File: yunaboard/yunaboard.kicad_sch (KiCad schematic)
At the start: 49 parts, among them J1 USB-C Receptacle USB 2.0, J2 JTAG/SWD Tag Connect, J3 PCB ANT, J4 GPIO Header 1, J5 GPIO Header 2, U1 ESP32-S3, U2 CP2102N-Axx-xQFN28, U3 USBLC6-2SC6, U4 MIC5365-3.3YD5, Y1 40 MHz (±10ppm)

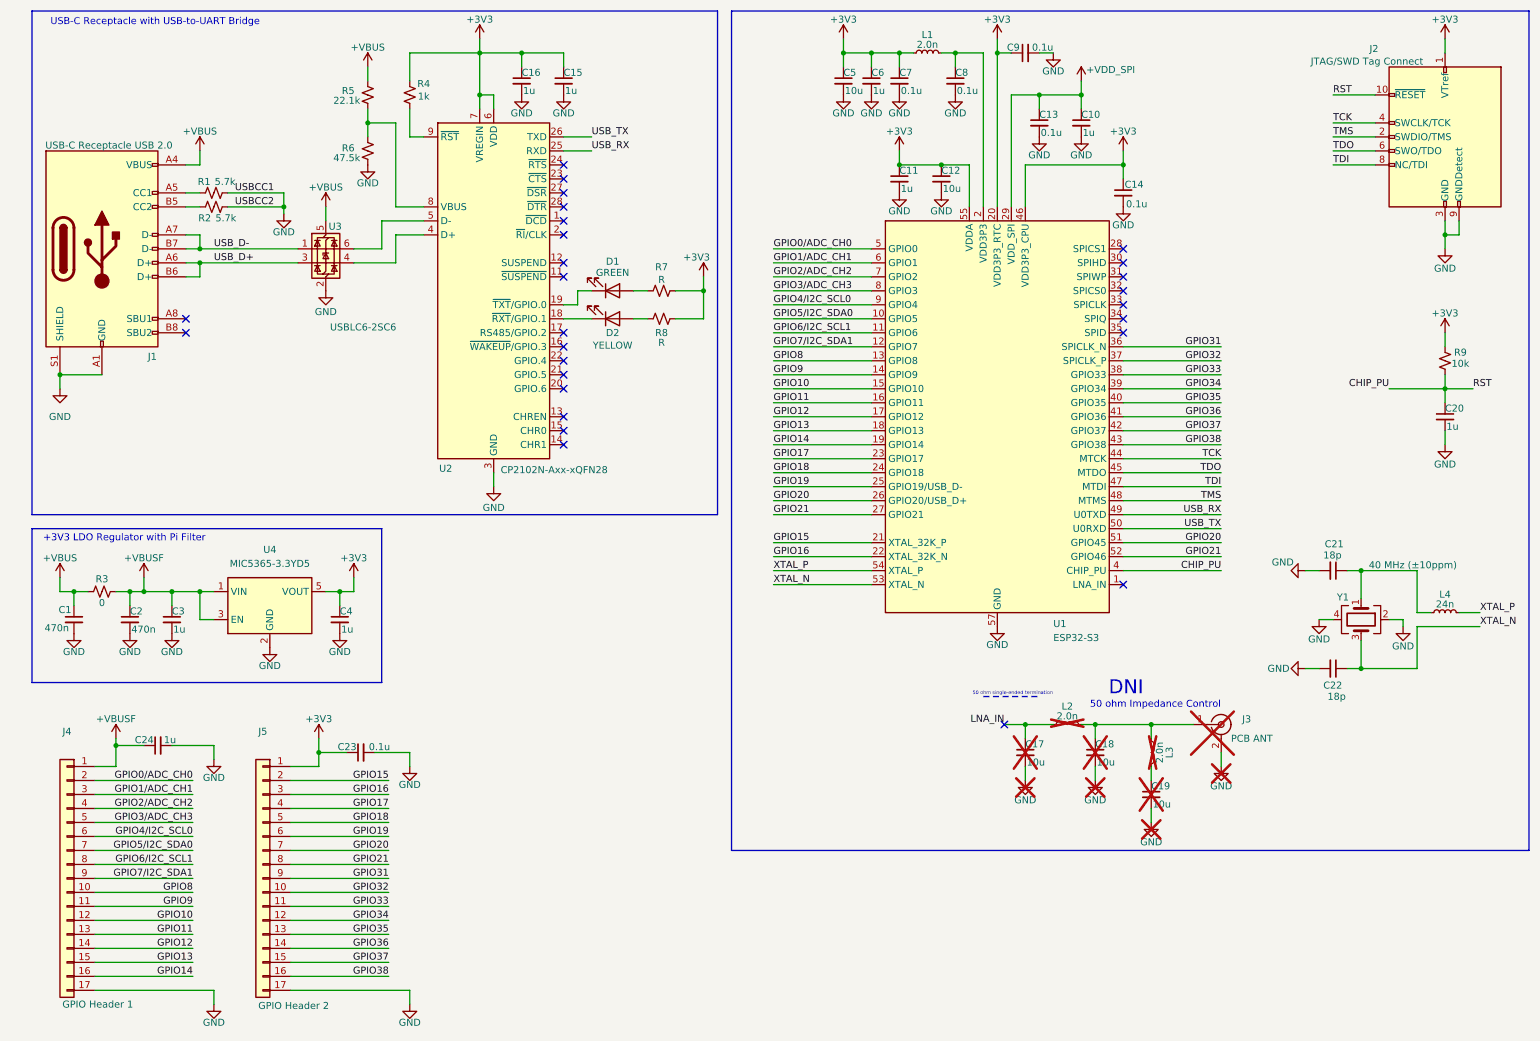
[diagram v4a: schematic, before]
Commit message: Update
- Changed JTAG connector to pin header for SWD
- Changed GPIO pin headers from 1mm length to 2mm length
- Adjusted the layout of the PCB from the initial design
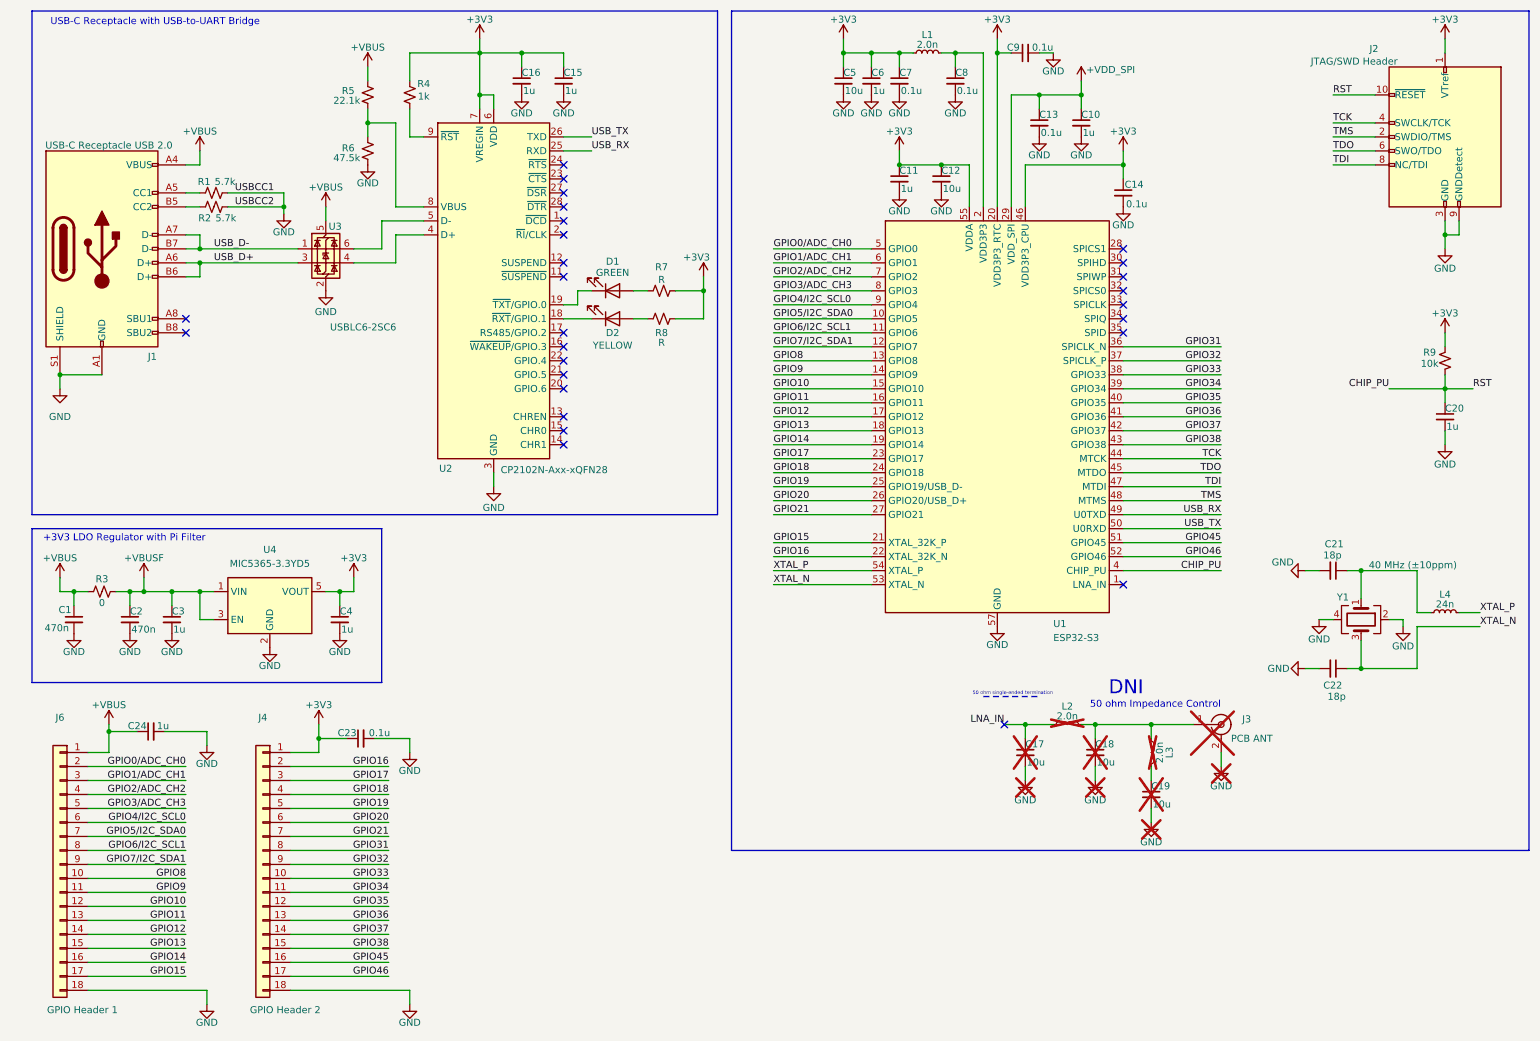
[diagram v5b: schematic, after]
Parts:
- removed J4: GPIO Header 1, Connector_PinHeader_1.00mm:PinHeader_1x17_P1.00mm_Vertical, symbol Connector_Generic:Conn_01x17
- removed J5: GPIO Header 2, Connector_PinHeader_1.00mm:PinHeader_1x17_P1.00mm_Vertical, symbol Connector_Generic:Conn_01x17
- added J4: GPIO Header 2, Connector_PinHeader_2.00mm:PinHeader_1x18_P2.00mm_Vertical, symbol Connector_Generic:Conn_01x18
- added J6: GPIO Header 1, Connector_PinHeader_2.00mm:PinHeader_1x18_P2.00mm_Vertical, symbol Connector_Generic:Conn_01x18
- J2: value JTAG/SWD Tag Connect -> JTAG/SWD Header; footprint Connector:Tag-Connect_TC2070-IDC-FP_2x07_P1.27mm_Vertical -> Connector_PinHeader_1.27mm:PinHeader_2x06_P1.27mm_Vertical
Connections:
- net +3V3: now also J4.1 (Pin_1)
- net +VBUS: now also C24.1, J6.1 (Pin_1)
- net +VBUSF: no longer C24.1
- net GND: now also J4.18 (Pin_18), J6.18 (Pin_18)
- net GPIO0/ADC_CH0: now also J6.2 (Pin_2)
- net GPIO10: now also J6.12 (Pin_12)
- net GPIO11: now also J6.13 (Pin_13)
- net GPIO12: now also J6.14 (Pin_14)
- net GPIO13: now also J6.15 (Pin_15)
- net GPIO14: now also J6.16 (Pin_16)
- net GPIO15: now also J6.17 (Pin_17)
- net GPIO16: now also J4.2 (Pin_2)
- net GPIO17: now also J4.3 (Pin_3)
- net GPIO18: now also J4.4 (Pin_4)
- net GPIO19: now also J4.5 (Pin_5)
- net GPIO1/ADC_CH1: now also J6.3 (Pin_3)
- net GPIO20: now also J4.6 (Pin_6); no longer U1.51 (GPIO45)
- net GPIO21: now also J4.7 (Pin_7); no longer U1.52 (GPIO46)
- net GPIO2/ADC_CH2: now also J6.4 (Pin_4)
- net GPIO31: now also J4.8 (Pin_8)
- net GPIO32: now also J4.9 (Pin_9)
- net GPIO33: now also J4.10 (Pin_10)
- net GPIO34: now also J4.11 (Pin_11)
- net GPIO35: now also J4.12 (Pin_12)
- net GPIO36: now also J4.13 (Pin_13)
- net GPIO37: now also J4.14 (Pin_14)
- net GPIO38: now also J4.15 (Pin_15)
- net GPIO3/ADC_CH3: now also J6.5 (Pin_5)
- net GPIO4/I2C_SCL0: now also J6.6 (Pin_6)
- net GPIO5/I2C_SDA0: now also J6.7 (Pin_7)
- net GPIO6/I2C_SCL1: now also J6.8 (Pin_8)
- net GPIO7/I2C_SDA1: now also J6.9 (Pin_9)
- net GPIO8: now also J6.10 (Pin_10)
- net GPIO9: now also J6.11 (Pin_11)
- new net GPIO45: J4.16 (Pin_16), U1.51 (GPIO45)
- new net GPIO46: J4.17 (Pin_17), U1.52 (GPIO46)
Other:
- moved on the sheet: C23, C24, R9

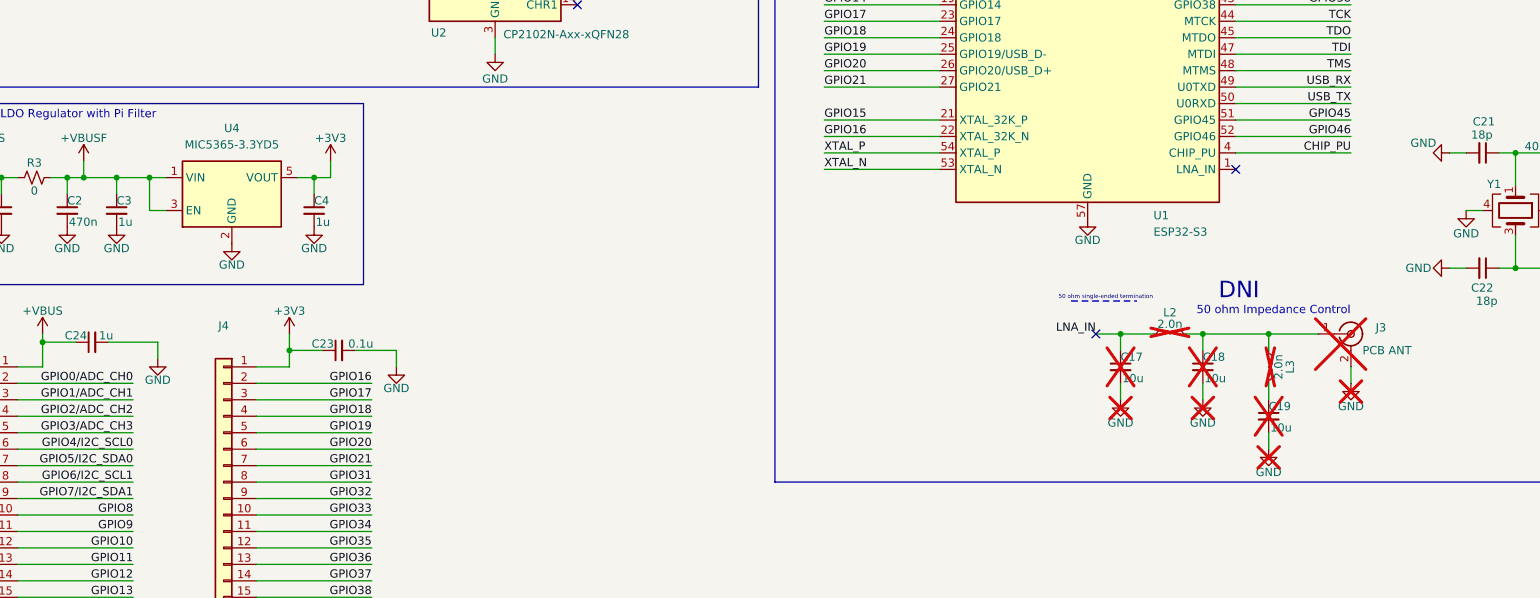
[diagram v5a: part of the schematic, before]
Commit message: Finalzed PCB
- Changed LDO to TLV75533PDBVR for an output current of 500 mA
- Adjusted some  routing to reduce ground plane breaking
- Adjusted some 3V3 traces to be 0.5mm instead of 0.3mm
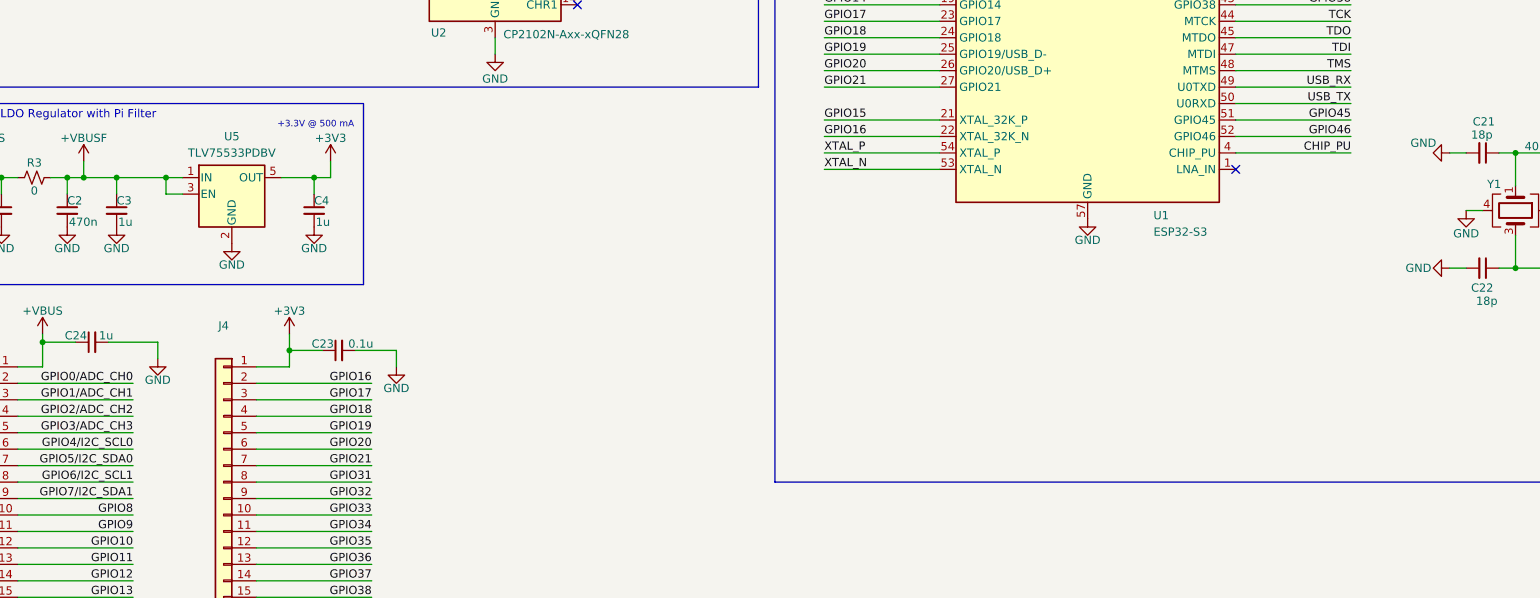
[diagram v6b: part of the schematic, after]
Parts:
- removed C17, C18, C19: 10u, Capacitor_SMD:C_0603_1608Metric, symbol Device:C_Small
- removed J3: PCB ANT, Connector_Coaxial:U.FL_Hirose_U.FL-R-SMT-1_Vertical, symbol Connector:Conn_Coaxial
- removed L2, L3: 2.0n, Inductor_SMD:L_0201_0603Metric, symbol Device:L_Small
- removed U4: MIC5365-3.3YD5, Package_TO_SOT_SMD:TSOT-23-5, symbol Regulator_Linear:MIC5365-3.3YD5
- added U5: TLV75533PDBV, Package_TO_SOT_SMD:SOT-23-5, symbol Regulator_Linear:TLV75533PDBV
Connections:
- net +3V3: now also U5.5 (OUT)
- net +VBUSF: now also U5.1 (IN), U5.3 (EN)
- net GND: now also U5.2 (GND)
- no-connect marks 27 -> 26
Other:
- note added: "+3.3V @ 500 mA"
- note removed: "50 ohm Impedance Control"
- note removed: "50 ohm single-ended termination"
- note removed: "DNI"
